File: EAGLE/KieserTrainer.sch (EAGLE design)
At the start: 14 parts, among them U1 ATMEGA328P-PU

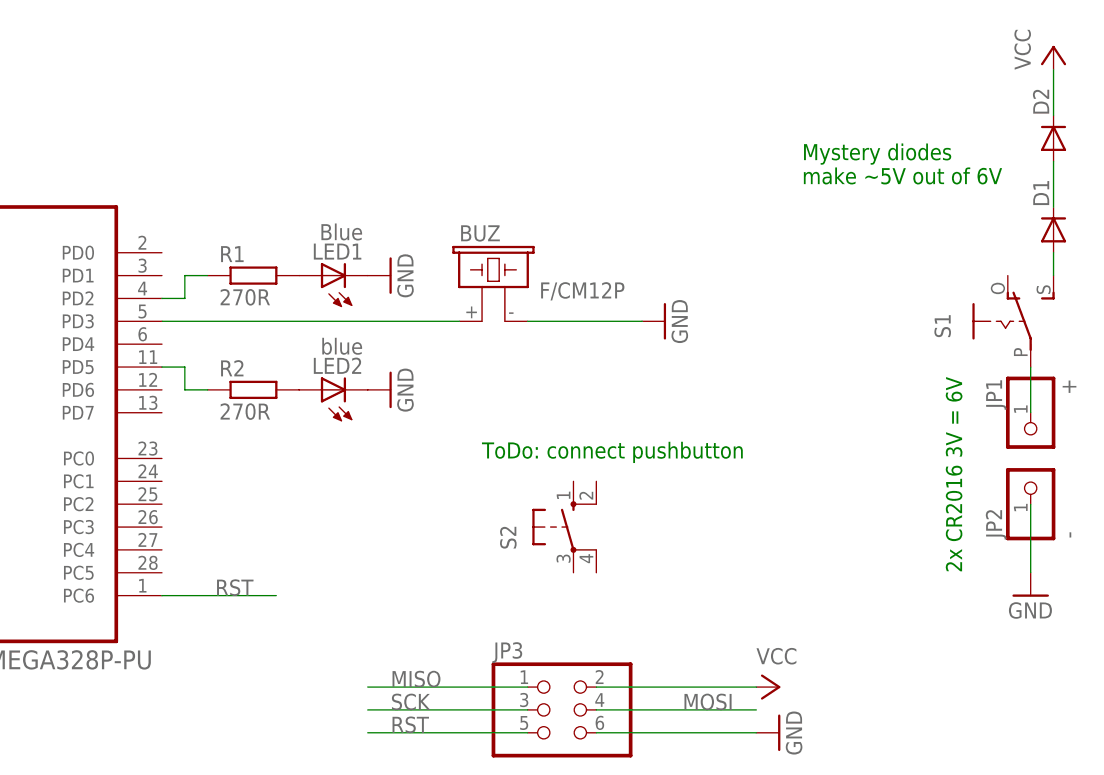
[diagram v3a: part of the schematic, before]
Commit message: Add board layout to match physical design
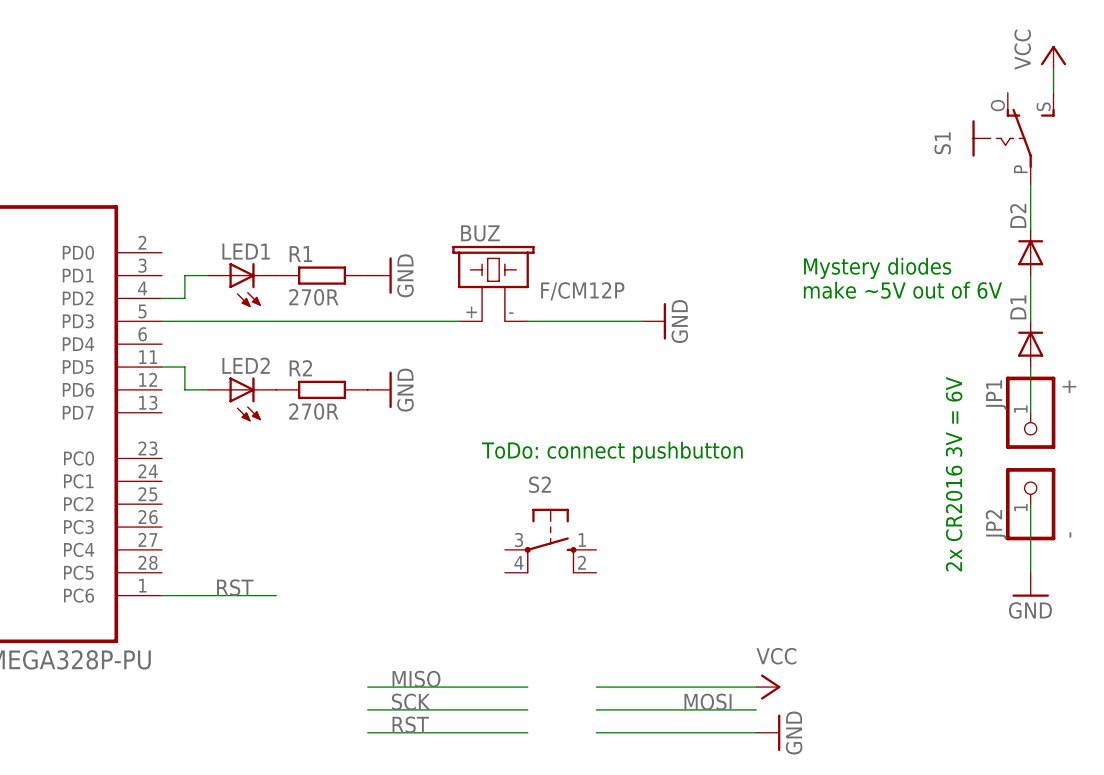
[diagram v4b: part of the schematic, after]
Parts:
- removed JP3: (no value), pinhead:PINHD-2X3
- LED1: value Blue -> (none); device adafruit:LEDCHIPLED_0805 -> led:LED3MM
- LED2: value blue -> (none); device adafruit:LEDCHIPLED_0805 -> led:LED3MM
- S2: device adafruit:40-XX -> switch-omron:10-XX
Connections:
- net GND: now also R1.2, R2.2; no longer JP3.6, LED1.C, LED2.C
- net MISO: no longer JP3.1
- net MOSI: no longer JP3.4
- net N$1: now also LED1.C, R1.1; no longer R2.1, U1.PD5
- net N$2: now also LED2.C, R2.1; no longer LED2.A, R2.2
- net N$3: now also U1.PD2; no longer R1.2
- net N$4: now also LED2.A, U1.PD5; no longer R1.1, U1.PD2
- net N$6: now also JP1.1; no longer S1.S
- net N$7: now also D2.C; no longer JP1.1
- net RST: no longer JP3.5
- net SCK: no longer JP3.3
- net VCC: now also S1.S; no longer D2.C, JP3.2
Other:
- moved on the sheet: D1, D2, LED1, LED2, R1, R2, S1, S2
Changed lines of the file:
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@@
 <part name="U1" library="Atmel_By_element14_Batch_1-00" deviceset="ATMEGA328P-PU" device=""/>
 <part name="BUZ" library="buzzer" deviceset="F/CM12P" device=""/>
-<part name="LED1" library="adafruit" deviceset="LED" device="CHIPLED_0805" value="Blue"/>
-<part name="LED2" library="adafruit" deviceset="LED" device="CHIPLED_0805" value="blue"/>
 <part name="R1" library="rcl" deviceset="R-EU_" device="R0805" value="270R"/>
 <part name="R2" library="rcl" deviceset="R-EU_" device="R0805" value="270R"/>
@@
 <part name="P+1" library="supply1" deviceset="VCC" device=""/>
 <part name="GND5" library="supply1" deviceset="GND" device=""/>
-<part name="JP3" library="pinhead" deviceset="PINHD-2X3" device=""/>
 <part name="P+2" library="supply1" deviceset="VCC" device=""/>
 <part name="GND6" library="supply1" deviceset="GND" device=""/>
 <part name="S1" library="adafruit" deviceset="EG1218" device="S"/>
-<part name="S2" library="adafruit" deviceset="40-XX" device=""/>
 <part name="P+3" library="supply1" deviceset="VCC" device=""/>
 <part name="D1" library="diode" deviceset="DIODE-" device="D-7.5"/>
@@
 <part name="P+4" library="supply1" deviceset="VCC" device=""/>
 <part name="GND7" library="supply1" deviceset="GND" device=""/>
+<part name="LED1" library="led" deviceset="LED" device="3MM"/>
+<part name="LED2" library="led" deviceset="LED" device="3MM"/>
+<part name="S2" library="switch-omron" deviceset="10-XX" device=""/>
 </parts>
 <sheets>
@@
 <plain>
 <text x="104.14" y="53.34" size="1.778" layer="91">ToDo: connect pushbutton</text>
-<text x="139.7" y="83.82" size="1.778" layer="91">Mystery diodes
+<text x="139.7" y="71.12" size="1.778" layer="91">Mystery diodes
 make ~5V out of 6V</text>
 <text x="157.48" y="40.64" size="1.778" layer="91" rot="R90">2x CR2016 3V = 6V</text>
@@
 <instance part="U1" gate="A" x="50.8" y="60.96"/>
 <instance part="BUZ" gate="G$1" x="104.14" y="71.12"/>
-<instance part="LED1" gate="G$1" x="86.36" y="73.66" rot="R90"/>
-<instance part="LED2" gate="G$1" x="86.36" y="60.96" rot="R90"/>
-<instance part="R1" gate="G$1" x="78.74" y="73.66"/>
-<instance part="R2" gate="G$1" x="78.74" y="60.96"/>
+<instance part="R1" gate="G$1" x="86.36" y="73.66"/>
+<instance part="R2" gate="G$1" x="86.36" y="60.96"/>
 <instance part="JP1" gate="G$1" x="165.1" y="55.88" rot="MR270"/>
 <instance part="JP2" gate="G$1" x="165.1" y="50.8" rot="R90"/>
@@
 <instance part="P+1" gate="VCC" x="30.48" y="81.28"/>
 <instance part="GND5" gate="1" x="124.46" y="68.58" rot="R90"/>
-<instance part="JP3" gate="A" x="111.76" y="25.4"/>
 <instance part="P+2" gate="VCC" x="137.16" y="27.94" rot="R270"/>
 <instance part="GND6" gate="1" x="137.16" y="22.86" rot="R90"/>
-<instance part="S1" gate="1" x="162.56" y="68.58"/>
-<instance part="S2" gate="1" x="114.3" y="45.72"/>
+<instance part="S1" gate="1" x="162.56" y="88.9"/>
 <instance part="P+3" gate="VCC" x="167.64" y="99.06"/>
-<instance part="D1" gate="G$1" x="167.64" y="78.74" rot="R90"/>
-<instance part="D2" gate="G$1" x="167.64" y="88.9" rot="R90"/>
+<instance part="D1" gate="G$1" x="165.1" y="66.04" rot="R90"/>
+<instance part="D2" gate="G$1" x="165.1" y="76.2" rot="R90"/>
 <instance part="C1" gate="G$1" x="10.16" y="68.58"/>
 <instance part="P+4" gate="VCC" x="10.16" y="73.66"/>
 <instance part="GND7" gate="1" x="10.16" y="60.96"/>
+<instance part="LED1" gate="G$1" x="76.2" y="73.66" rot="R90"/>
+<instance part="LED2" gate="G$1" x="76.2" y="60.96" rot="R90"/>
+<instance part="S2" gate="1" x="111.76" y="43.18" rot="R270"/>
 </instances>
 <busses>
@@
 </segment>
 <segment>
-<pinref part="GND1" gate="1" pin="GND"/>
-<pinref part="LED1" gate="G$1" pin="C"/>
-</segment>
-<segment>
-<pinref part="GND2" gate="1" pin="GND"/>
-<pinref part="LED2" gate="G$1" pin="C"/>
-</segment>
-<segment>
-<pinref part="JP3" gate="A" pin="6"/>
 <wire x1="116.84" y1="22.86" x2="134.62" y2="22.86" width="0.1524" layer="91"/>
 <pinref part="GND6" gate="1" pin="GND"/>
@@
 <pinref part="C1" gate="G$1" pin="2"/>
 <pinref part="GND7" gate="1" pin="GND"/>
+</segment>
+<segment>
+<pinref part="GND1" gate="1" pin="GND"/>
+<pinref part="R1" gate="G$1" pin="2"/>
+</segment>
+<segment>
+<pinref part="GND2" gate="1" pin="GND"/>
+<pinref part="R2" gate="G$1" pin="2"/>
 </segment>
 </net>
@@
 </segment>
 <segment>
-<pinref part="JP3" gate="A" pin="2"/>
 <wire x1="116.84" y1="27.94" x2="134.62" y2="27.94" width="0.1524" layer="91"/>
 <pinref part="P+2" gate="VCC" pin="VCC"/>
 </segment>
 <segment>
-<pinref part="D2" gate="G$1" pin="C"/>
-<pinref part="P+3" gate="VCC" pin="VCC"/>
-<wire x1="167.64" y1="96.52" x2="167.64" y2="91.44" width="0.1524" layer="91"/>
-</segment>
-<segment>
 <pinref part="C1" gate="G$1" pin="1"/>
 <pinref part="P+4" gate="VCC" pin="VCC"/>
 </segment>
-</net>
-<net name="N$2" class="0">
-<segment>
-<pinref part="LED2" gate="G$1" pin="A"/>
-<pinref part="R2" gate="G$1" pin="2"/>
+<segment>
+<pinref part="S1" gate="1" pin="S"/>
+<pinref part="P+3" gate="VCC" pin="VCC"/>
+<wire x1="167.64" y1="93.98" x2="167.64" y2="96.52" width="0.1524" layer="91"/>
 </segment>
 </net>
@@
 </segment>
 <segment>
-<pinref part="JP3" gate="A" pin="5"/>
 <wire x1="109.22" y1="22.86" x2="91.44" y2="22.86" width="0.1524" layer="91"/>
 <label x="93.98" y="22.86" size="1.778" layer="95"/>
@@
 </segment>
 <segment>
-<pinref part="JP3" gate="A" pin="4"/>
 <wire x1="116.84" y1="25.4" x2="134.62" y2="25.4" width="0.1524" layer="91"/>
 <label x="132.08" y="25.4" size="1.778" layer="95" rot="MR0"/>
@@
 </segment>
 <segment>
-<pinref part="JP3" gate="A" pin="1"/>
 <wire x1="109.22" y1="27.94" x2="91.44" y2="27.94" width="0.1524" layer="91"/>
 <label x="93.98" y="27.94" size="1.778" layer="95"/>
@@
 </segment>
 <segment>
-<pinref part="JP3" gate="A" pin="3"/>
 <wire x1="109.22" y1="25.4" x2="91.44" y2="25.4" width="0.1524" layer="91"/>
 <label x="93.98" y="25.4" size="1.778" layer="95"/>
-</segment>
-</net>
-<net name="N$3" class="0">
-<segment>
-<pinref part="R1" gate="G$1" pin="2"/>
-<pinref part="LED1" gate="G$1" pin="A"/>
-</segment>
-</net>
-<net name="N$4" class="0">
-<segment>
-<pinref part="U1" gate="A" pin="PD2"/>
-<pinref part="R1" gate="G$1" pin="1"/>
-<wire x1="73.66" y1="73.66" x2="71.12" y2="73.66" width="0.1524" layer="91"/>
-<wire x1="71.12" y1="73.66" x2="71.12" y2="71.12" width="0.1524" layer="91"/>
-<wire x1="71.12" y1="71.12" x2="68.58" y2="71.12" width="0.1524" layer="91"/>
 </segment>
 </net>
@@
 </segment>
 </net>
-<net name="N$1" class="0">
-<segment>
-<pinref part="U1" gate="A" pin="PD5"/>
-<pinref part="R2" gate="G$1" pin="1"/>
-<wire x1="73.66" y1="60.96" x2="71.12" y2="60.96" width="0.1524" layer="91"/>
-<wire x1="71.12" y1="60.96" x2="71.12" y2="63.5" width="0.1524" layer="91"/>
-<wire x1="71.12" y1="63.5" x2="68.58" y2="63.5" width="0.1524" layer="91"/>
-</segment>
-</net>
-<net name="N$7" class="0">
-<segment>
-<pinref part="JP1" gate="G$1" pin="1"/>
-<pinref part="S1" gate="1" pin="P"/>
-<wire x1="165.1" y1="58.42" x2="165.1" y2="63.5" width="0.1524" layer="91"/>
-</segment>
-</net>
-<net name="N$6" class="0">
-<segment>
-<pinref part="S1" gate="1" pin="S"/>
-<pinref part="D1" gate="G$1" pin="A"/>
-<wire x1="167.64" y1="76.2" x2="167.64" y2="73.66" width="0.1524" layer="91"/>
-</segment>
-</net>
 <net name="N$8" class="0">
 <segment>
 <pinref part="D1" gate="G$1" pin="C"/>
 <pinref part="D2" gate="G$1" pin="A"/>
-<wire x1="167.64" y1="86.36" x2="167.64" y2="81.28" width="0.1524" layer="91"/>
-</segment>
-</net>
+<wire x1="165.1" y1="73.66" x2="165.1" y2="68.58" width="0.1524" layer="91"/>
+</segment>
+</net>
+<net name="N$3" class="0">
+<segment>
+<wire x1="73.66" y1="73.66" x2="71.12" y2="73.66" width="0.1524" layer="91"/>
+<wire x1="71.12" y1="73.66" x2="71.12" y2="71.12" width="0.1524" layer="91"/>
+<pinref part="U1" gate="A" pin="PD2"/>
+<wire x1="71.12" y1="71.12" x2="68.58" y2="71.12" width="0.1524" layer="91"/>
+<pinref part="LED1" gate="G$1" pin="A"/>
+</segment>
+</net>
+<net name="N$4" class="0">
+<segment>
+<pinref part="U1" gate="A" pin="PD5"/>
+<wire x1="68.58" y1="63.5" x2="71.12" y2="63.5" width="0.1524" layer="91"/>
+<wire x1="71.12" y1="63.5" x2="71.12" y2="60.96" width="0.1524" layer="91"/>
+<wire x1="71.12" y1="60.96" x2="73.66" y2="60.96" width="0.1524" layer="91"/>
+<pinref part="LED2" gate="G$1" pin="A"/>
+</segment>
+</net>
+<net name="N$1" class="0">
+<segment>
+<pinref part="R1" gate="G$1" pin="1"/>
+<pinref part="LED1" gate="G$1" pin="C"/>
+</segment>
+</net>
+<net name="N$2" class="0">
+<segment>
+<pinref part="R2" gate="G$1" pin="1"/>
+<pinref part="LED2" gate="G$1" pin="C"/>
+</segment>
+</net>
+<net name="N$6" class="0">
+<segment>
+<pinref part="JP1" gate="G$1" pin="1"/>
+<pinref part="D1" gate="G$1" pin="A"/>
+<wire x1="165.1" y1="63.5" x2="165.1" y2="58.42" width="0.1524" layer="91"/>
+</segment>
+</net>
+<net name="N$7" class="0">
+<segment>
+<pinref part="D2" gate="G$1" pin="C"/>
+<pinref part="S1" gate="1" pin="P"/>
+<wire x1="165.1" y1="78.74" x2="165.1" y2="83.82" width="0.1524" layer="91"/>
+</segment>
+</net>

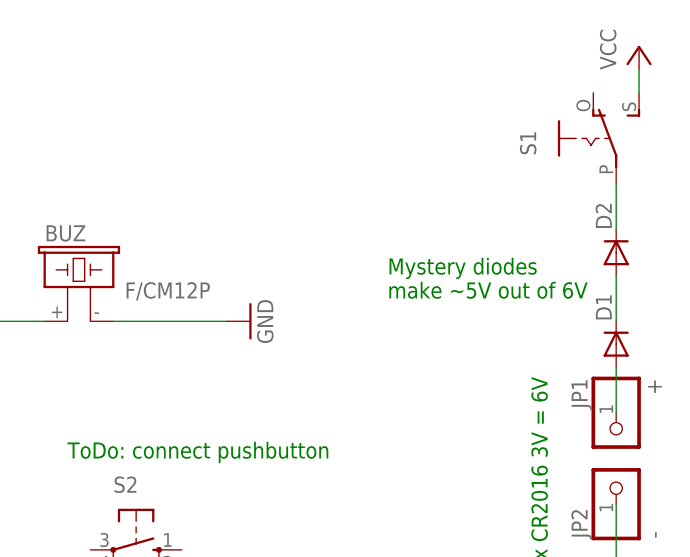
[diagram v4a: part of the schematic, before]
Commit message: Bypass mystery diodes to feed ATmega with full 6V (exactly the max rating, but oh well)
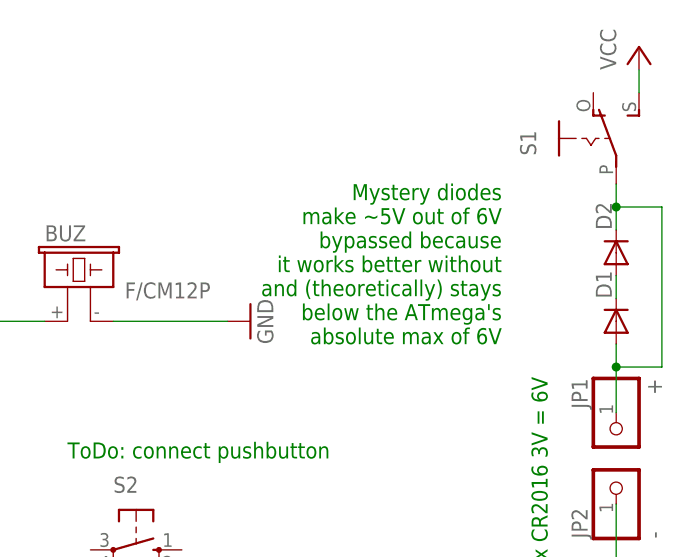
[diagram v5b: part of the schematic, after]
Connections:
- removed net N$7: D2.C, S1.P
- net N$6: now also D2.C, S1.P
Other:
- note added: "Mystery diodes make ~5V out of 6V bypassed because it works better without and (theoretically) stays below the ATmega's absolute max of 6V"
- note removed: "Mystery diodes make ~5V out of 6V"
- moved on the sheet: D1
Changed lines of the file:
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@@
 <plain>
 <text x="104.14" y="53.34" size="1.778" layer="91">ToDo: connect pushbutton</text>
-<text x="139.7" y="71.12" size="1.778" layer="91">Mystery diodes
-make ~5V out of 6V</text>
+<text x="152.4" y="66.04" size="1.778" layer="91" align="bottom-right">Mystery diodes
+make ~5V out of 6V
+bypassed because
+it works better without
+and (theoretically) stays
+below the ATmega's
+absolute max of 6V</text>
 <text x="157.48" y="40.64" size="1.778" layer="91" rot="R90">2x CR2016 3V = 6V</text>
 </plain>
@@
 <instance part="S1" gate="1" x="162.56" y="88.9"/>
 <instance part="P+3" gate="VCC" x="167.64" y="99.06"/>
-<instance part="D1" gate="G$1" x="165.1" y="66.04" rot="R90"/>
+<instance part="D1" gate="G$1" x="165.1" y="68.58" rot="R90"/>
 <instance part="D2" gate="G$1" x="165.1" y="76.2" rot="R90"/>
 <instance part="C1" gate="G$1" x="10.16" y="68.58"/>
@@
 <pinref part="D1" gate="G$1" pin="C"/>
 <pinref part="D2" gate="G$1" pin="A"/>
-<wire x1="165.1" y1="73.66" x2="165.1" y2="68.58" width="0.1524" layer="91"/>
+<wire x1="165.1" y1="73.66" x2="165.1" y2="71.12" width="0.1524" layer="91"/>
 </segment>
 </net>
@@
 <pinref part="JP1" gate="G$1" pin="1"/>
 <pinref part="D1" gate="G$1" pin="A"/>
+<wire x1="165.1" y1="66.04" x2="165.1" y2="63.5" width="0.1524" layer="91"/>
 <wire x1="165.1" y1="63.5" x2="165.1" y2="58.42" width="0.1524" layer="91"/>
-</segment>
-</net>
-<net name="N$7" class="0">
-<segment>
+<wire x1="165.1" y1="63.5" x2="170.18" y2="63.5" width="0.1524" layer="91"/>
+<wire x1="170.18" y1="63.5" x2="170.18" y2="81.28" width="0.1524" layer="91"/>
 <pinref part="D2" gate="G$1" pin="C"/>
 <pinref part="S1" gate="1" pin="P"/>
-<wire x1="165.1" y1="78.74" x2="165.1" y2="83.82" width="0.1524" layer="91"/>
-</segment>
-</net>
+<wire x1="165.1" y1="78.74" x2="165.1" y2="81.28" width="0.1524" layer="91"/>
+<wire x1="165.1" y1="81.28" x2="165.1" y2="83.82" width="0.1524" layer="91"/>
+<wire x1="170.18" y1="81.28" x2="165.1" y2="81.28" width="0.1524" layer="91"/>
+<junction x="165.1" y="63.5"/>
+<junction x="165.1" y="81.28"/>
+</segment>
+</net>

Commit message: Add been/no beep feature, implement hardware interrupt for waking, rewire push button and LED
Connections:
- new net N$7: S2.S1, U1.PD2
- net GND: now also S2.P1
- net N$3: now also U1.PD1; no longer U1.PD2
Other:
- note removed: "ToDo: connect pushbutton"
- moved on the sheet: S2
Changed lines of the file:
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@@
 <part name="LED2" library="led" deviceset="LED" device="3MM"/>
 <part name="S2" library="switch-omron" deviceset="10-XX" device=""/>
+<part name="GND8" library="supply1" deviceset="GND" device=""/>
 </parts>
 <sheets>
 <sheet>
 <plain>
-<text x="104.14" y="53.34" size="1.778" layer="91">ToDo: connect pushbutton</text>
 <text x="152.4" y="66.04" size="1.778" layer="91" align="bottom-right">Mystery diodes
 make ~5V out of 6V
@@
 <instance part="LED1" gate="G$1" x="76.2" y="73.66" rot="R90"/>
 <instance part="LED2" gate="G$1" x="76.2" y="60.96" rot="R90"/>
-<instance part="S2" gate="1" x="111.76" y="43.18" rot="R270"/>
+<instance part="S2" gate="1" x="81.28" y="91.44" rot="MR270"/>
+<instance part="GND8" gate="1" x="91.44" y="86.36"/>
 </instances>
 <busses>
@@
 <pinref part="R2" gate="G$1" pin="2"/>
 </segment>
+<segment>
+<pinref part="GND8" gate="1" pin="GND"/>
+<pinref part="S2" gate="1" pin="P1"/>
+<wire x1="86.36" y1="88.9" x2="91.44" y2="88.9" width="0.1524" layer="91"/>
+</segment>
 </net>
 <net name="VCC" class="0">
@@
 <pinref part="D2" gate="G$1" pin="A"/>
 <wire x1="165.1" y1="73.66" x2="165.1" y2="71.12" width="0.1524" layer="91"/>
-</segment>
-</net>
-<net name="N$3" class="0">
-<segment>
-<wire x1="73.66" y1="73.66" x2="71.12" y2="73.66" width="0.1524" layer="91"/>
-<wire x1="71.12" y1="73.66" x2="71.12" y2="71.12" width="0.1524" layer="91"/>
-<pinref part="U1" gate="A" pin="PD2"/>
-<wire x1="71.12" y1="71.12" x2="68.58" y2="71.12" width="0.1524" layer="91"/>
-<pinref part="LED1" gate="G$1" pin="A"/>
 </segment>
 </net>
@@
 </segment>
 </net>
+<net name="N$3" class="0">
+<segment>
+<pinref part="LED1" gate="G$1" pin="A"/>
+<pinref part="U1" gate="A" pin="PD1"/>
+<wire x1="73.66" y1="73.66" x2="68.58" y2="73.66" width="0.1524" layer="91"/>
+</segment>
+</net>
+<net name="N$7" class="0">
+<segment>
+<pinref part="U1" gate="A" pin="PD2"/>
+<wire x1="68.58" y1="71.12" x2="71.12" y2="71.12" width="0.1524" layer="91"/>
+<wire x1="71.12" y1="71.12" x2="71.12" y2="88.9" width="0.1524" layer="91"/>
+<pinref part="S2" gate="1" pin="S1"/>
+<wire x1="76.2" y1="88.9" x2="71.12" y2="88.9" width="0.1524" layer="91"/>
+</segment>
+</net>
